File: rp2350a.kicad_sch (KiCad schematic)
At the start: 28 parts, among them U5 RP2350_60QFN, Y2 ASE-12.000MHz-E-T

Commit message: Assigned footprints and drew pcb outline
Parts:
- C1, C10, C11, C12, C13, C14, C16, C2, C3, C4, C5, C6, C7, C8, C9: footprint (none) -> Capacitor_Tantalum_SMD:CP_EIA-2012-15_AVX-P
- L1: footprint (none) -> Inductor_SMD:L_6.3x6.3_H3
- R1, R2, R20, R3, R4, R5, R6, R7, R8, R9: footprint Resistor_THT:R_Axial_DIN0207_L6.3mm_D2.5mm_P7.62mm_Horizontal -> Resistor_SMD:R_0805_2012Metric
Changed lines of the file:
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@@
 			)
 		)
-		(property "Footprint" "Resistor_THT:R_Axial_DIN0207_L6.3mm_D2.5mm_P7.62mm_Horizontal"
+		(property "Footprint" "Resistor_SMD:R_0805_2012Metric"
 			(at 143.51 89.408 90)
 			(effects
@@
 			)
 		)
-		(property "Footprint" "Resistor_THT:R_Axial_DIN0207_L6.3mm_D2.5mm_P7.62mm_Horizontal"
+		(property "Footprint" "Resistor_SMD:R_0805_2012Metric"
 			(at 128.27 46.228 90)
 			(effects
@@
 			)
 		)
-		(property "Footprint" "Resistor_THT:R_Axial_DIN0207_L6.3mm_D2.5mm_P7.62mm_Horizontal"
+		(property "Footprint" "Resistor_SMD:R_0805_2012Metric"
 			(at 238.76 58.928 90)
 			(effects
@@
 			)
 		)
-		(property "Footprint" ""
+		(property "Footprint" "Capacitor_Tantalum_SMD:CP_EIA-2012-15_AVX-P"
 			(at 49.2252 129.54 0)
 			(effects
@@
 			)
 		)
-		(property "Footprint" ""
+		(property "Footprint" "Capacitor_Tantalum_SMD:CP_EIA-2012-15_AVX-P"
 			(at 249.8852 40.64 0)
 			(effects
@@
 			)
 		)
-		(property "Footprint" "Resistor_THT:R_Axial_DIN0207_L6.3mm_D2.5mm_P7.62mm_Horizontal"
+		(property "Footprint" "Resistor_SMD:R_0805_2012Metric"
 			(at 92.202 115.57 90)
 			(effects
@@
 			)
 		)
-		(property "Footprint" ""
+		(property "Footprint" "Capacitor_Tantalum_SMD:CP_EIA-2012-15_AVX-P"
 			(at 243.5352 40.64 0)
 			(effects
@@
 			)
 		)
-		(property "Footprint" ""
+		(property "Footprint" "Capacitor_Tantalum_SMD:CP_EIA-2012-15_AVX-P"
 			(at 230.8352 40.64 0)
 			(effects
@@
 			)
 		)
-		(property "Footprint" "Resistor_THT:R_Axial_DIN0207_L6.3mm_D2.5mm_P7.62mm_Horizontal"
+		(property "Footprint" "Resistor_SMD:R_0805_2012Metric"
 			(at 143.51 91.948 90)
 			(effects
@@
 			)
 		)
-		(property "Footprint" ""
+		(property "Footprint" "Capacitor_Tantalum_SMD:CP_EIA-2012-15_AVX-P"
 			(at 211.7852 40.64 0)
 			(effects
@@
 			)
 		)
-		(property "Footprint" ""
+		(property "Footprint" "Capacitor_Tantalum_SMD:CP_EIA-2012-15_AVX-P"
 			(at 224.4852 40.64 0)
 			(effects
@@
 			)
 		)
-		(property "Footprint" "Resistor_THT:R_Axial_DIN0207_L6.3mm_D2.5mm_P7.62mm_Horizontal"
+		(property "Footprint" "Resistor_SMD:R_0805_2012Metric"
 			(at 143.51 86.868 90)
 			(effects
@@
 			)
 		)
-		(property "Footprint" "Resistor_THT:R_Axial_DIN0207_L6.3mm_D2.5mm_P7.62mm_Horizontal"
+		(property "Footprint" "Resistor_SMD:R_0805_2012Metric"
 			(at 143.51 95.758 90)
 			(effects
@@
 			)
 		)
-		(property "Footprint" ""
+		(property "Footprint" "Capacitor_Tantalum_SMD:CP_EIA-2012-15_AVX-P"
 			(at 111.4552 67.31 0)
 			(effects
@@
 			)
 		)
-		(property "Footprint" "Resistor_THT:R_Axial_DIN0207_L6.3mm_D2.5mm_P7.62mm_Horizontal"
+		(property "Footprint" "Resistor_SMD:R_0805_2012Metric"
 			(at 143.51 84.328 90)
 			(effects
@@
 			)
 		)
-		(property "Footprint" ""
+		(property "Footprint" "Capacitor_Tantalum_SMD:CP_EIA-2012-15_AVX-P"
 			(at 162.2552 33.02 0)
 			(effects
@@
 			)
 		)
-		(property "Footprint" ""
+		(property "Footprint" "Capacitor_Tantalum_SMD:CP_EIA-2012-15_AVX-P"
 			(at 98.7552 67.31 0)
 			(effects
@@
 			)
 		)
-		(property "Footprint" "Resistor_THT:R_Axial_DIN0207_L6.3mm_D2.5mm_P7.62mm_Horizontal"
+		(property "Footprint" "Resistor_SMD:R_0805_2012Metric"
 			(at 26.162 142.24 90)
 			(effects
@@
 			)
 		)
-		(property "Footprint" ""
+		(property "Footprint" "Inductor_SMD:L_6.3x6.3_H3"
 			(at 124.46 62.23 0)
 			(effects
@@
 			)
 		)
-		(property "Footprint" ""
+		(property "Footprint" "Capacitor_Tantalum_SMD:CP_EIA-2012-15_AVX-P"
 			(at 218.1352 40.64 0)
 			(effects
@@
 			)
 		)
-		(property "Footprint" ""
+		(property "Footprint" "Capacitor_Tantalum_SMD:CP_EIA-2012-15_AVX-P"
 			(at 94.9452 129.54 0)
 			(effects
@@
 			)
 		)
-		(property "Footprint" ""
+		(property "Footprint" "Capacitor_Tantalum_SMD:CP_EIA-2012-15_AVX-P"
 			(at 237.1852 40.64 0)
 			(effects
@@
 			)
 		)
-		(property "Footprint" ""
+		(property "Footprint" "Capacitor_Tantalum_SMD:CP_EIA-2012-15_AVX-P"
 			(at 155.9052 33.02 0)
 			(effects
@@
 			)
 		)
-		(property "Footprint" ""
+		(property "Footprint" "Capacitor_Tantalum_SMD:CP_EIA-2012-15_AVX-P"
 			(at 149.5552 33.02 0)
 			(effects
@@
 			)
 		)
-		(property "Footprint" "Resistor_THT:R_Axial_DIN0207_L6.3mm_D2.5mm_P7.62mm_Horizontal"
+		(property "Footprint" "Resistor_SMD:R_0805_2012Metric"
 			(at 238.76 57.912 90)
 			(effects
@@
 			)
 		)
-		(property "Footprint" ""
+		(property "Footprint" "Capacitor_Tantalum_SMD:CP_EIA-2012-15_AVX-P"
 			(at 143.2052 53.34 0)
 			(effects

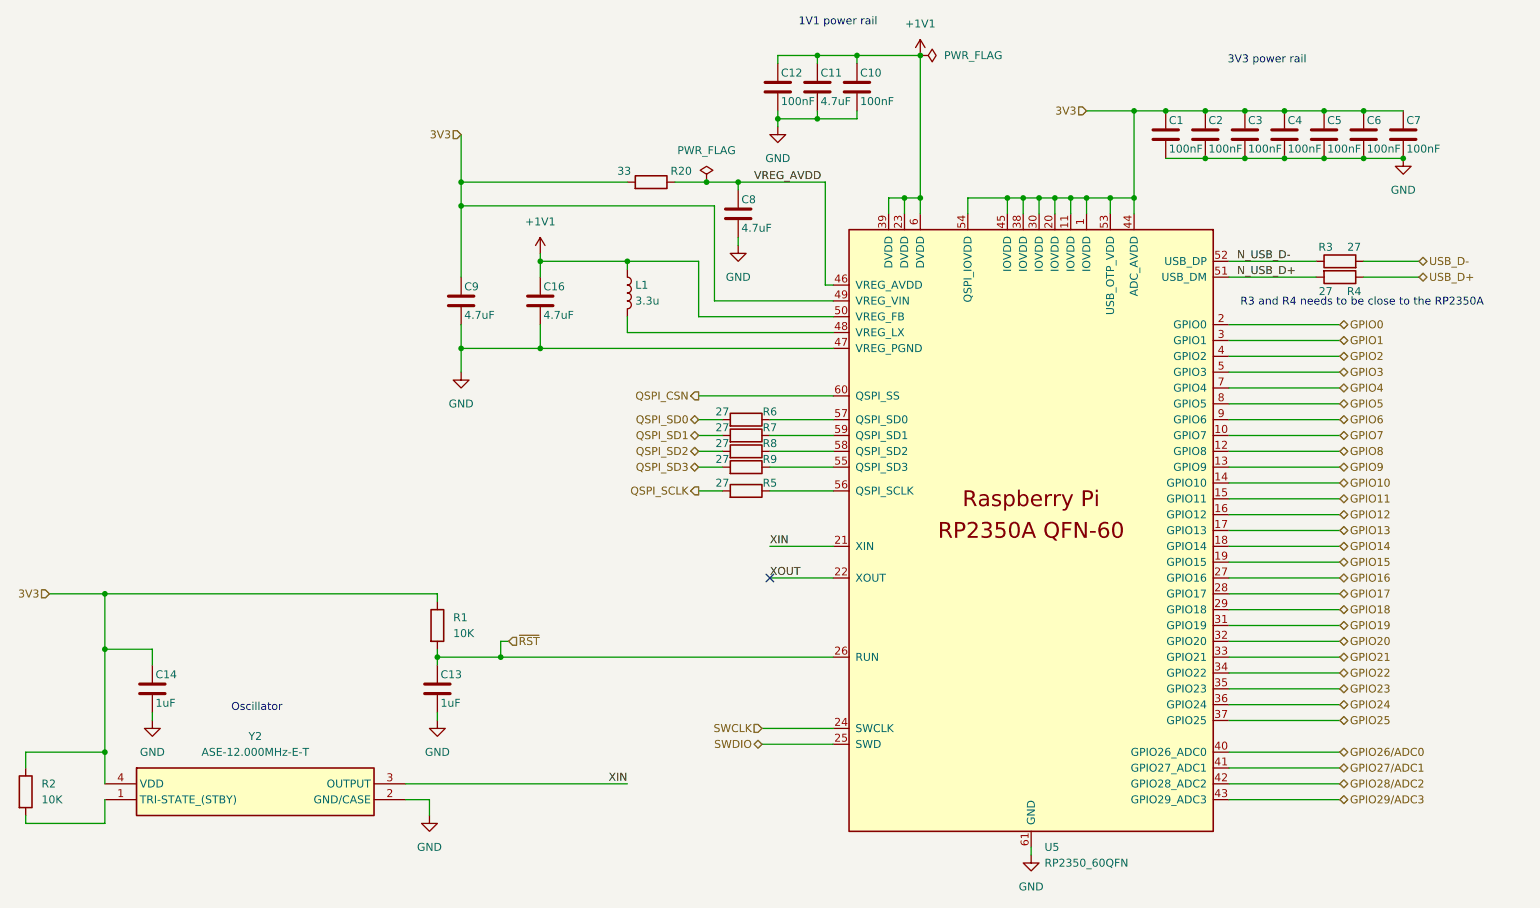
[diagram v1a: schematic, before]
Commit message: Fixed design flaw with with components that MCU depends on
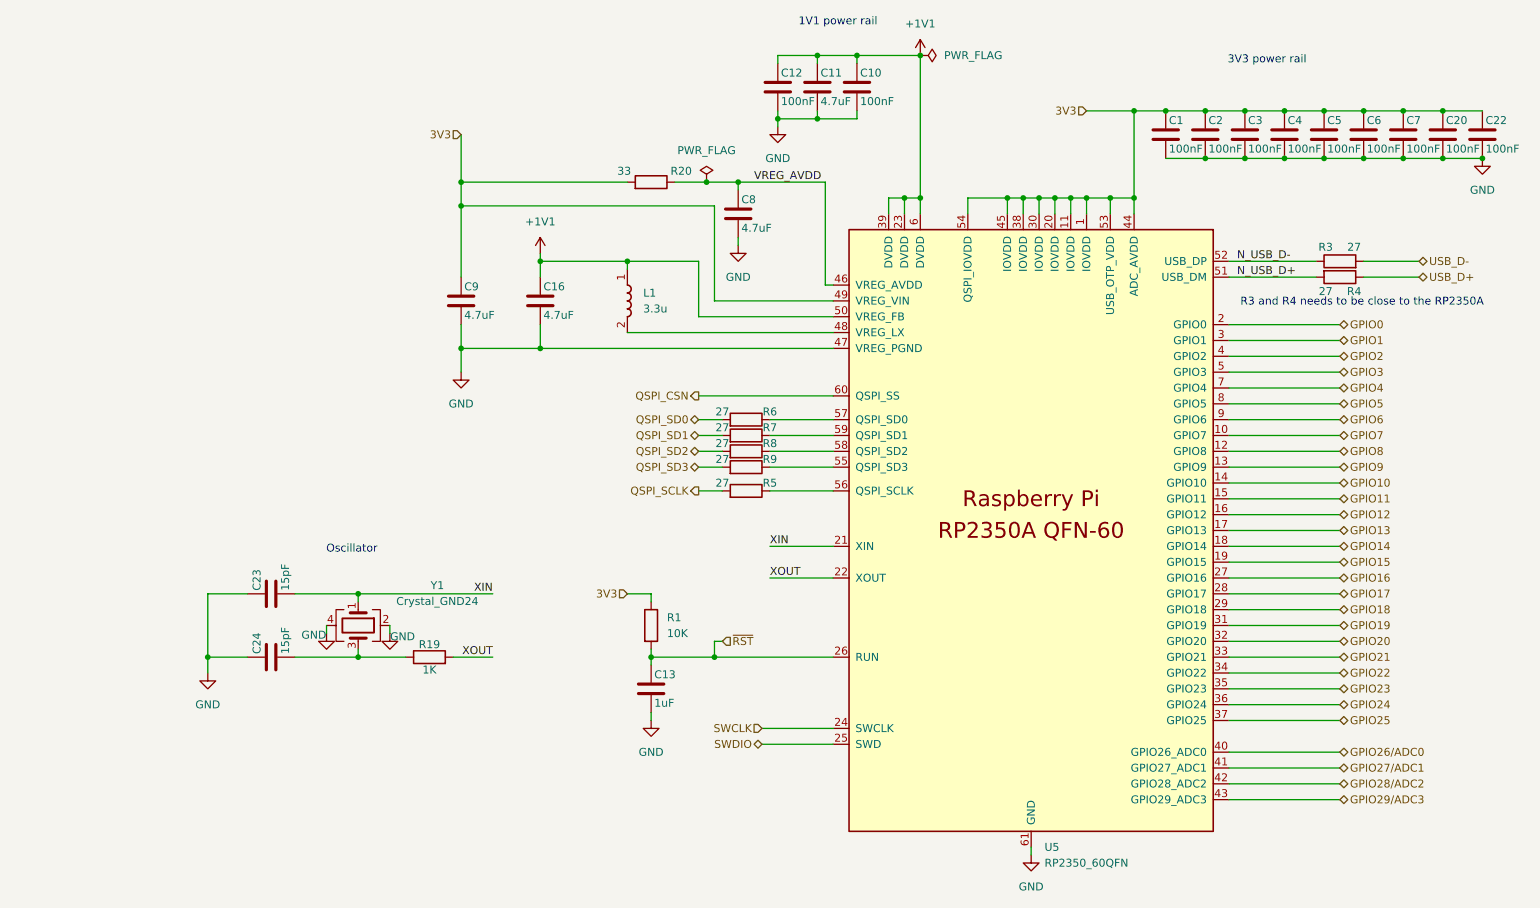
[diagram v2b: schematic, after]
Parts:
- removed C14: 1uF, Capacitor_Tantalum_SMD:CP_EIA-2012-15_AVX-P, symbol Device:C
- removed R2: 10K, Resistor_SMD:R_0805_2012Metric, symbol Device:R
- removed Y2: ASE-12.000MHz-E-T, SamacSys_Parts:ASE12000MHzET, symbol SamacSys_Parts:ASE-12.000MHz-E-T
- added C20, C22: 100nF, Capacitor_SMD:C_0402_1005Metric, symbol Device:C
- added C23, C24: 15pF, Capacitor_SMD:C_0402_1005Metric, symbol Device:C
- added R19: 1K, Resistor_SMD:R_0402_1005Metric, symbol Device:R
- added Y1: Crystal_GND24, clock:ABM8272T3, symbol Device:Crystal_GND24
- C1, C10, C11, C12, C16, C2, C3, C4, C5, C6, C7, C8, C9: footprint Capacitor_Tantalum_SMD:CP_EIA-2012-15_AVX-P -> Capacitor_SMD:C_0402_1005Metric
- L1: footprint Inductor_SMD:L_6.3x6.3_H3 -> inductors:AOTAB201610S3R3101T; symbol Device:L -> inductors:AOTA-B201610S3R3-101-T; Height (none) -> 1; Manufacturer_Name (none) -> ABRACON; Manufacturer_Part_Number (none) -> AOTA-B201610S3R3-101-T; Mouser Part Number (none) -> 815-AB201610S3R3101T; Mouser Price/Stock (none) -> https://www.mouser.co.uk/ProductDetail/ABRACON/AOTA-B201610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
- R20: footprint Resistor_SMD:R_0805_2012Metric -> Resistor_SMD:R_0402_1005Metric
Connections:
- net 3V3: now also C20.1, C22.1
- net GND: now also C20.2, C22.2, C23.1, C24.1, Y1.2, Y1.4
- net XIN: now also C23.2, Y1.1
- net XOUT: now also R19.2
- new net: C24.2, R19.1, Y1.3
- no-connect marks 1 -> 0
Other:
- moved on the sheet: C13, R1

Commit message: changed buzzer circuit and capacitor footprints
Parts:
- C13: footprint Capacitor_Tantalum_SMD:CP_EIA-2012-15_AVX-P -> Capacitor_SMD:C_0805_2012Metric
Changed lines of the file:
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@@
 			)
 		)
-		(property "Footprint" "Capacitor_Tantalum_SMD:CP_EIA-2012-15_AVX-P"
+		(property "Footprint" "Capacitor_SMD:C_0805_2012Metric"
 			(at 129.2352 129.54 0)
 			(effects

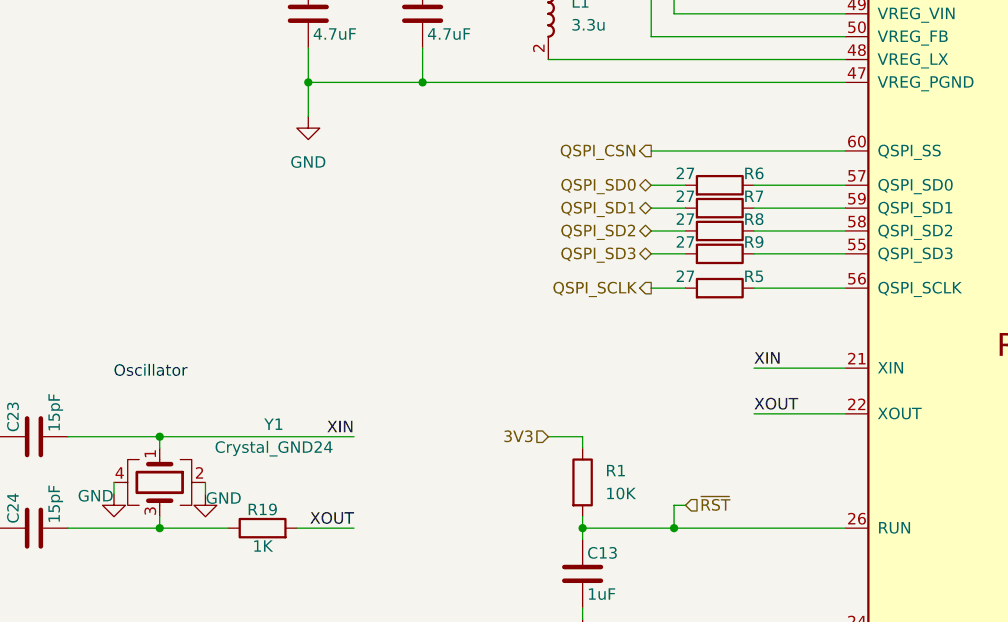
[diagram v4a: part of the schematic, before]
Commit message: Changed QSPI and added pull-ups on i2c
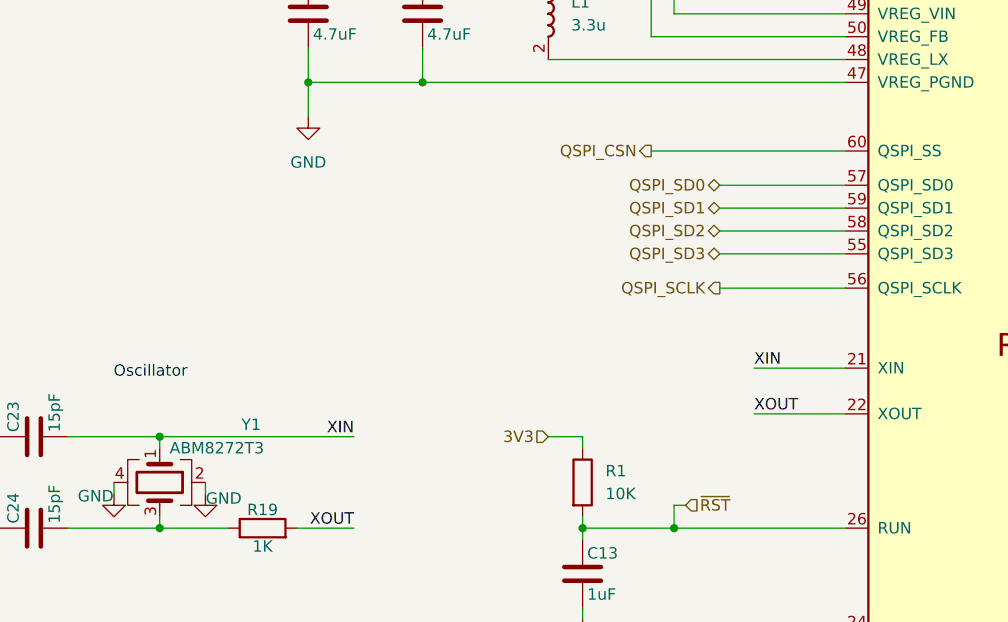
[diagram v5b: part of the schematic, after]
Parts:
- removed R5, R6, R7, R8, R9: 27, Resistor_SMD:R_0805_2012Metric, symbol Device:R
- Y1: value Crystal_GND24 -> ABM8272T3
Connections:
- net QSPI_SCLK: now also U5.56 (QSPI_SCLK)
- net QSPI_SD0: now also U5.57 (QSPI_SD0)
- net QSPI_SD1: now also U5.59 (QSPI_SD1)
- net QSPI_SD2: now also U5.58 (QSPI_SD2)
- net QSPI_SD3: now also U5.55 (QSPI_SD3)

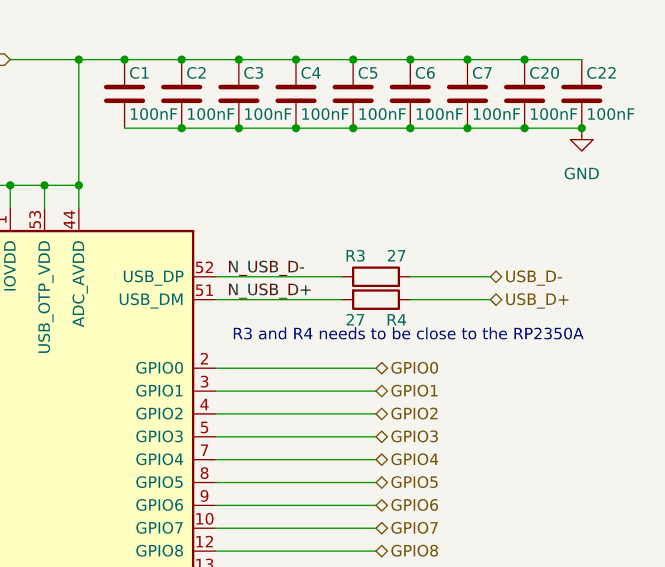
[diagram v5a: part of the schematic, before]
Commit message: Fixed USB data lines
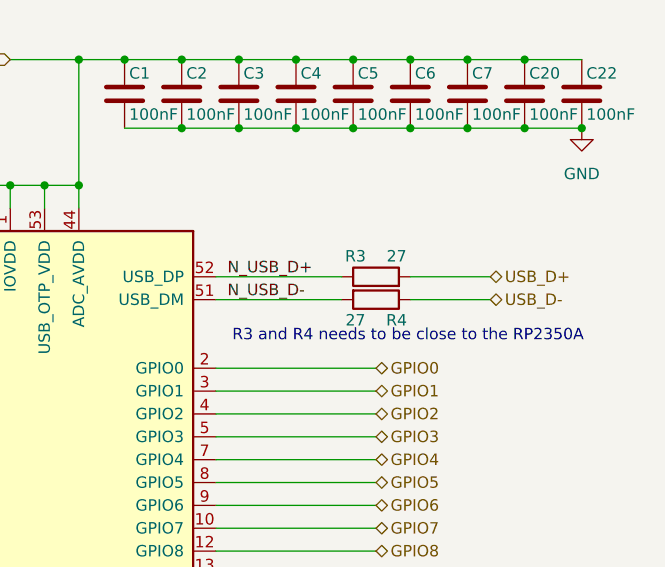
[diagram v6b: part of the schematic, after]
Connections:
- net N_USB_D+: now also R3.1, U5.52 (USB_DP); no longer R4.2, U5.51 (USB_DM)
- net N_USB_D-: now also R4.2, U5.51 (USB_DM); no longer R3.1, U5.52 (USB_DP)
- net USB_D+: now also R3.2; no longer R4.1
- net USB_D-: now also R4.1; no longer R3.2
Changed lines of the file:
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@@
 		)
 	)
-	(label "N_USB_D-"
+	(label "N_USB_D+"
 		(at 222.25 57.15 0)
 		(effects
@@
 		)
 	)
-	(label "N_USB_D+"
+	(label "N_USB_D-"
 		(at 222.25 59.69 0)
 		(effects
@@
 		)
 	)
-	(hierarchical_label "USB_D+"
+	(hierarchical_label "USB_D-"
 		(shape bidirectional)
 		(at 251.46 59.69 0)
@@
 		)
 	)
-	(hierarchical_label "USB_D-"
+	(hierarchical_label "USB_D+"
 		(shape bidirectional)
 		(at 251.46 57.15 0)
